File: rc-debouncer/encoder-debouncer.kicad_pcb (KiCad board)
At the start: 2 copper layers, 58.4 x 31.8 mm, 29 parts, among them J1 MCU, J2 SIG.IN, SW1 Input, U1 LM311, U2 LM358

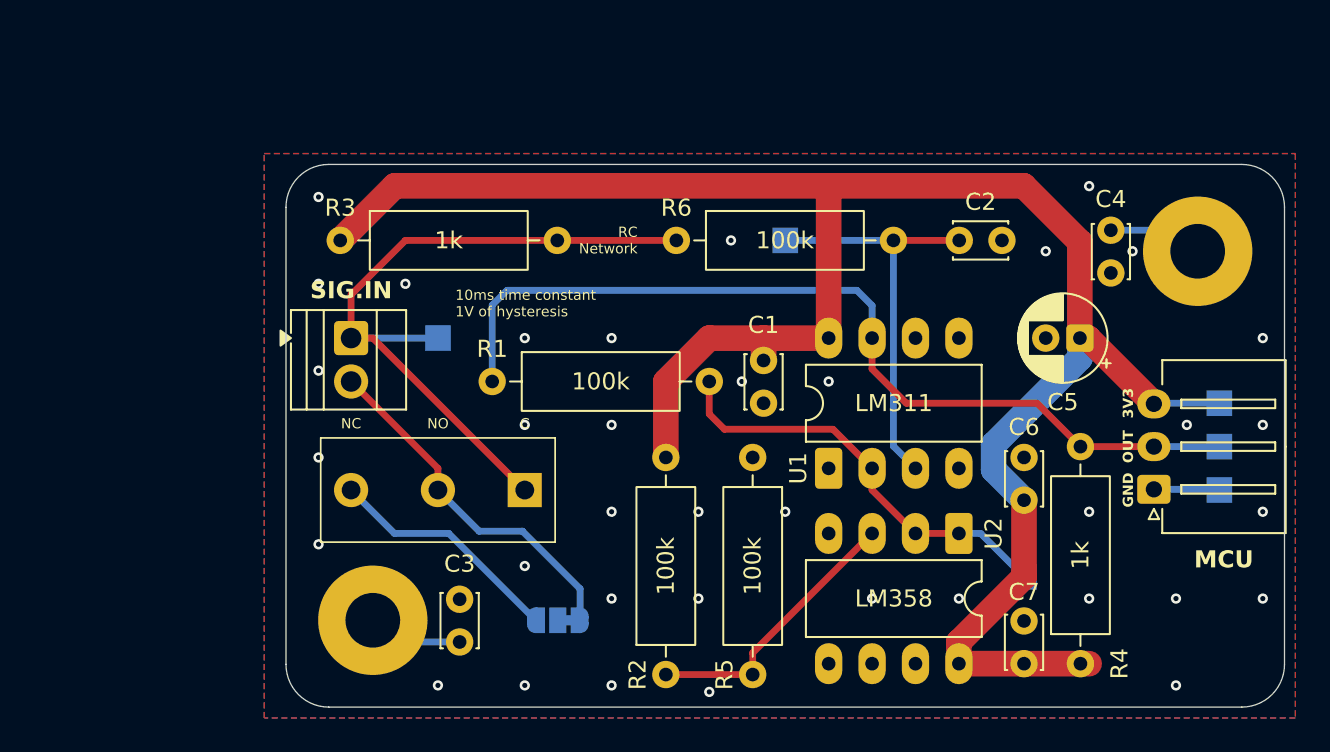
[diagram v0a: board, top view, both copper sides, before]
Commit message: Finish new layout
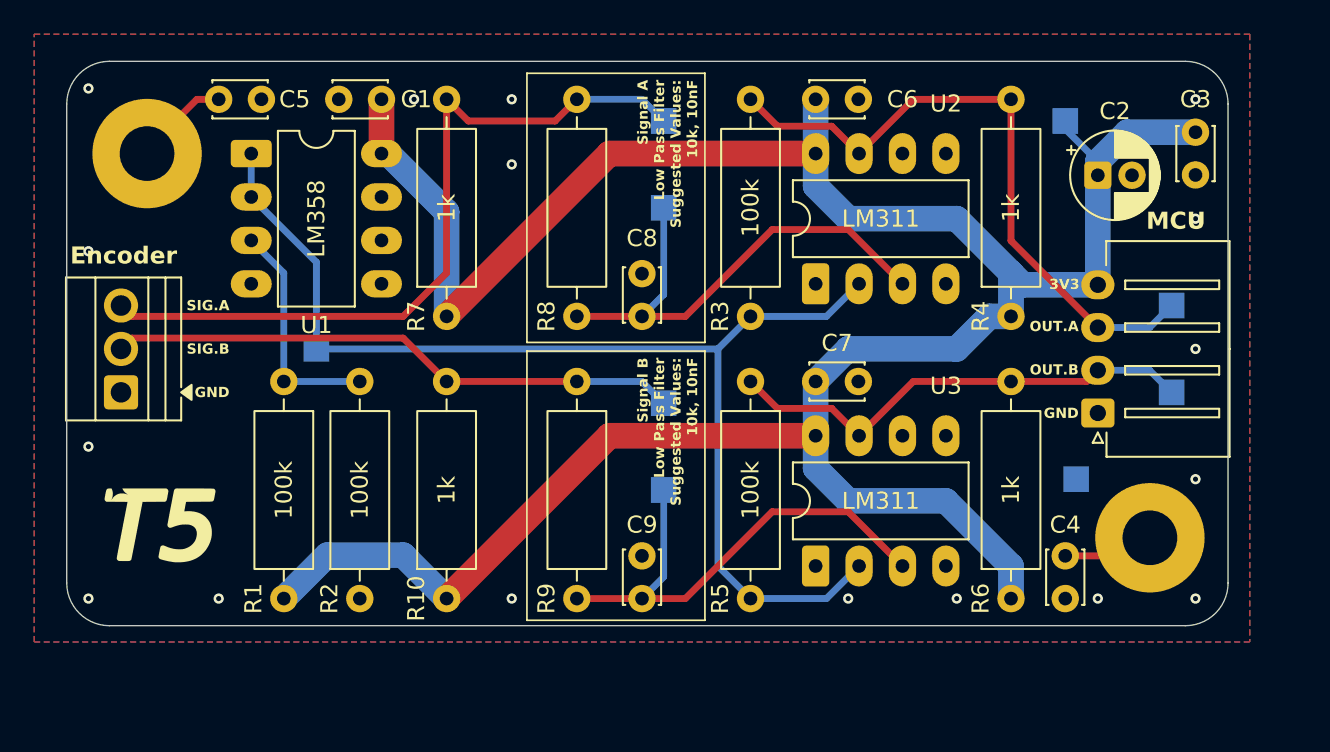
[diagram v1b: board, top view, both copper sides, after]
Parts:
- removed JP1: SW_INVERSION, Jumper:SolderJumper-3_P1.3mm_Bridged12_RoundedPad1.0x1.5mm
- removed the REF** at (203.8, 88.3)
- removed SW1: Input, Button_Switch_THT:SW_XKB_DM1-16UP-1
- added C8: 10nF, Capacitor_THT:C_Disc_D3.0mm_W2.0mm_P2.50mm, F.Cu at (215.1, 92.7)
- added C9: 10nF, Capacitor_THT:C_Disc_D3.0mm_W2.0mm_P2.50mm, F.Cu at (215.1, 109.2)
- added R10: 1k, Resistor_THT:R_Axial_DIN0309_L9.0mm_D3.2mm_P12.70mm_Horizontal, F.Cu at (203.7, 109.2)
- added R7: 1k, Resistor_THT:R_Axial_DIN0309_L9.0mm_D3.2mm_P12.70mm_Horizontal, F.Cu at (203.7, 92.7)
- added R8: 10k, Resistor_THT:R_Axial_DIN0309_L9.0mm_D3.2mm_P12.70mm_Horizontal, F.Cu at (211.3, 80.0)
- added R9: 10k, Resistor_THT:R_Axial_DIN0309_L9.0mm_D3.2mm_P12.70mm_Horizontal, F.Cu at (211.3, 96.5)
- added REF**: OSHW-Logo_5.7x6mm_SilkScreen, Symbol:OSHW-Logo_5.7x6mm_SilkScreen, B.Cu at (207.5, 88.9)
- added S2: Logo, GS_Virtual:ENPH253_Logo, B.Cu at (188.5, 104.1)
- added TP7: SIG_B.OUT, TestPoint:TestPoint_Pad_1.5x1.5mm, B.Cu at (246.1, 97.2)
- added TP8: 3.3V, TestPoint:TestPoint_Pad_1.5x1.5mm, B.Cu at (239.9, 81.3)
- added TP9: GND, TestPoint:TestPoint_Pad_1.5x1.5mm, B.Cu at (240.5, 102.2)
- added U3: LM311, Package_DIP:DIP-8_W7.62mm_LongPads, F.Cu at (225.3, 107.3)
- C2: value 100nF -> 10uF; footprint Capacitor_THT:C_Disc_D3.0mm_W2.0mm_P2.50mm -> Capacitor_THT:CP_Radial_D5.0mm_P2.00mm
- C5: value 10uF -> 100nF; footprint Capacitor_THT:CP_Radial_D5.0mm_P2.00mm -> Capacitor_THT:C_Disc_D3.0mm_W2.0mm_P2.50mm
- J1: value MCU -> Encoder; footprint GS_Connectors:JST_XH_S3B-XH-A-1_1x03_P2.50mm_Horizontal -> TerminalBlock:TerminalBlock_Xinya_XY308-2.54-3P_1x03_P2.54mm_Horizontal
- J2: value SIG.IN -> MCU; footprint TerminalBlock:TerminalBlock_Xinya_XY308-2.54-2P_1x02_P2.54mm_Horizontal -> GS_Connectors:JST_XH_S4B-XH-A-1_1x04_P2.50mm_Horizontal
- R3: value 1k -> 100k
- R6: value 100k -> 1k
- S1: footprint GS_Virtual:ENPH253_Logo -> GS_Virtual:ENPH253_Logo_Small; moved to F.Cu
- TP1: value 3.3V -> SIG_A.RAW
- TP2: value GND -> SIG_A.RC_FILTERED
- TP3: value SIG.RC_FILTERED -> SIG_A.OUT
- TP4: value SIG.RAW -> V_REF
- TP5: value V_REF -> SIG_B.RAW
- TP6: value SIG.OUT -> SIG_B.RC_FILTERED
- U1: value LM311 -> LM358
- U2: value LM358 -> LM311
- moved H2 61.7 mm to (186.2, 83.2)
- moved J1 60.7 mm to (184.7, 97.2)
- moved S1 59.3 mm to (187.2, 104.8), turned to 0 degrees
- moved C3 52.4 mm to (247.5, 81.9), turned to -90 degrees
- moved C5 52.3 mm to (190.4, 80.0), turned to 0 degrees
- moved H1 45.7 mm to (244.9, 105.7)
- moved J2 43.9 mm to (241.8, 98.4), turned to 90 degrees
- moved U1 38.5 mm to (192.3, 83.2), turned to 0 degrees
- moved TP1 36.5 mm to (216.4, 81.3), turned to 0 degrees
- moved TP2 36.5 mm to (216.4, 86.4), turned to 0 degrees
- moved TP6 32.6 mm to (216.4, 102.9), turned to 0 degrees
- moved R6 28.7 mm to (236.7, 109.2), turned to 90 degrees
- moved C1 27.1 mm to (199.9, 80.0), turned to 180 degrees
- moved C6 26.4 mm to (225.3, 80.0), turned to 0 degrees
- moved R3 25.4 mm to (221.5, 80.0), turned to -90 degrees
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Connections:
- C2 pad 1: Net-(U1--) -> +3.3V
- C3 pad 1: Net-(C3-Pad1) -> +3.3V
- C5 pad 1: +3.3V -> Net-(C5-Pad1)
- H1 pad 1: Net-(C3-Pad1) -> Net-(C4-Pad1)
- H2 pad 1: Net-(C4-Pad1) -> Net-(C5-Pad1)
- J1 pad 2: /SIG.OUT -> /SIG_B.IN
- J1 pad 3: +3.3V -> /SIG_A.IN
- J2 pad 1: Net-(J2-Pin_1) -> GND
- J2 pad 2: Net-(J2-Pin_2) -> /SIG_B.OUT
- R1 pad 1: /SIG.OUT -> Net-(U1A-+)
- R1 pad 2: Net-(U1-+) -> +3.3V
- R2 pad 1: Net-(U2A-+) -> GND
- R2 pad 2: +3.3V -> Net-(U1A-+)
- R3 pad 1: +3.3V -> /SIG_A.OUT
- R3 pad 2: Net-(J2-Pin_1) -> /V_REF
- R4 pad 2: /SIG.OUT -> /SIG_A.OUT
- R5 pad 1: GND -> /SIG_B.OUT
- R5 pad 2: Net-(U2A-+) -> /V_REF
- R6 pad 1: Net-(J2-Pin_1) -> +3.3V
- R6 pad 2: Net-(U1--) -> /SIG_B.OUT
- TP1 pad 1: +3.3V -> /SIG_A.IN
- TP2 pad 1: GND -> /RC low pass network A/V_OUT
- TP3 pad 1: Net-(U1--) -> /SIG_A.OUT
- TP4 pad 1: Net-(J2-Pin_1) -> /V_REF
- TP5 pad 1: Net-(U1-+) -> /SIG_B.IN
- TP6 pad 1: /SIG.OUT -> /RC low pass network B/V_OUT
- U1 pad 1: GND -> /V_REF
- U1 pad 2: Net-(U1-+) -> /V_REF
- U1 pad 3: Net-(U1--) -> Net-(U1A-+)
- U1 pad 7: /SIG.OUT -> unconnected-(U1-Pad7)
- U2 pad 1: Net-(U1-+) -> GND
- U2 pad 2: Net-(U1-+) -> /V_REF
- U2 pad 3: Net-(U2A-+) -> /RC low pass network A/V_OUT
- U2 pad 7: unconnected-(U2-Pad7) -> /SIG_A.OUT
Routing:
- net /V_REF: track 0.00 -> 68.9 mm
- net /SIG.OUT: track 53.3 -> 0.00 mm
- net /SIG_A.IN: track 0.00 -> 44.8 mm
- net Net-(J2-Pin_1): track 41.8 -> 0.00 mm
- net /SIG_A.OUT: track 0.00 -> 38.2 mm
- net +3.3V: track 117.6 -> 154.3 mm
- net /SIG_B.IN: track 0.00 -> 33.6 mm
- net /RC low pass network A/V_OUT: track 0.00 -> 29.3 mm
- net /RC low pass network B/V_OUT: track 0.00 -> 29.3 mm
- net /SIG_B.OUT: track 0.00 -> 28.1 mm
- net Net-(U1-+): track 25.0 -> 0.00 mm
- net Net-(U1--): track 24.0 -> 0.00 mm
- net Net-(J2-Pin_2): track 21.0 -> 0.00 mm
- net Net-(U2A-+): track 16.2 -> 0.00 mm
- net Net-(JP1-B): track 14.0 -> 0.00 mm
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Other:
- board size 58.4 x 31.8 mm -> 67.9 x 33 mm
- board text added: "1.1V of hysteresis"
- board text added: "67.9450 mm x 33.0200 mm"
- board text added: "Encoder Debouncer"
- board text added: "OUT.A"
- board text added: "OUT.B"
- board text added: "SIG.A"
- board text added: "SIG.B"
- board text added: "Signal A Low Pass Filter Suggested Values: 10k, 10nF"
- board text added: "Signal B Low Pass Filter Suggested Values: 10k, 10nF"
- board text added: "github.com/ enph253-2025-team5/ encoder-debouncing-pcb"
- board text removed: "10ms time constant 1V of hysteresis"
- board text removed: "58.4200 mm x 31.7500 mm"
- board text removed: "C"
- board text removed: "NC"
- board text removed: "NO"
- board text removed: "OUT"
- board text removed: "RC Debouncer"
- board text removed: "RC Network"
- board text removed: "github.com /enph253-2025-team5 /rc-debouncing-pcb"
